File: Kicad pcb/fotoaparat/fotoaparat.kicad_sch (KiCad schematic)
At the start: 69 parts, among them IC1 Lineární Regulátor, IC2 Lineární Regulátor Displaye, J1 USB Konektor, J2 SWD, J3 LCD konektor, J4 Baterie, J5 Sd Karta, J6 UART, J7 Kamera, J8 Volné Piny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

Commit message: Buzzer
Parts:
- removed J8: Volné Piny, symbol Connector:Conn_01x12_Socket
- added BZ1: Buzzer, Inductor_SMD:L_SXN_SMDRI73, symbol Device:Buzzer
- added J9: Conn_01x11_Socket, symbol Connector:Conn_01x11_Socket
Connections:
- net -BATT: now also BZ1.2 (-)
- net pa10: now also J9.7 (Pin_7)
- net pa15: now also J9.3 (Pin_3)
- net pa2: now also J9.4 (Pin_4)
- net pa8: now also J9.5 (Pin_5)
- net pa9: now also J9.6 (Pin_6)
- net pb0: now also J9.2 (Pin_2)
- net pb1: now also J9.1 (Pin_1)
- net pb12: now also J9.10 (Pin_10)
- net pb14: now also J9.11 (Pin_11)
- net pc10: now also J9.8 (Pin_8)
- net pd2: now also J9.9 (Pin_9)
- net pb15 renamed buzzer
- net buzzer: now also BZ1.1 (+)
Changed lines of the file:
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@@
 	(wire
 		(pts
+			(xy 257.81 166.37) (xy 255.27 166.37)
+		)
+		(stroke
+			(width 0)
+			(type default)
+		)
+	)
+	(wire
+		(pts
 			(xy 129.54 55.88) (xy 116.84 55.88)
 		)
@@
 	(wire
 		(pts
-			(xy 179.07 161.29) (xy 252.73 161.29)
+			(xy 179.07 161.29) (xy 257.81 161.29)
 		)
 		(stroke
@@
 	(wire
 		(pts
-			(xy 252.73 161.29) (xy 252.73 135.89)
-		)
-		(stroke
-			(width 0)
-			(type default)
-		)
-	)
-	(wire
-		(pts
 			(xy -72.39 196.85) (xy -71.12 196.85)
 		)
@@
 	(wire
 		(pts
+			(xy 255.27 166.37) (xy 255.27 168.91)
+		)
+		(stroke
+			(width 0)
+			(type default)
+		)
+	)
+	(wire
+		(pts
 			(xy 154.94 31.75) (xy 163.83 31.75)
 		)
@@
 		)
 	)
-	(label "pb15"
-		(at 252.73 143.51 0)
+	(label "buzzer"
+		(at 251.46 161.29 0)
 		(effects
 			(font
@@
 	)
 	(symbol
+		(lib_id "Device:Buzzer")
+		(at 260.35 163.83 0)
+		(unit 1)
+		(exclude_from_sim no)
+		(in_bom yes)
+		(on_board yes)
+		(dnp no)
+		(fields_autoplaced yes)
+		(property "Reference" "BZ1"
+			(at 264.16 162.5599 0)
+			(effects
+				(font
+					(size 1.27 1.27)
+				)
+				(justify left)
+			)
+		)
+		(property "Value" "Buzzer"
+			(at 264.16 165.0999 0)
+			(effects
+				(font
+					(size 1.27 1.27)
+				)
+				(justify left)
+			)
+		)
+		(property "Footprint" "Inductor_SMD:L_SXN_SMDRI73"
+			(at 259.715 161.29 90)
+			(effects
+				(font
+					(size 1.27 1.27)
+				)
+				(hide yes)
+			)
+		)
+		(property "Datasheet" "~"
+			(at 259.715 161.29 90)
+			(effects
+				(font
+					(size 1.27 1.27)
+				)
+				(hide yes)
+			)
+		)
+		(property "Description" "Buzzer, polarized"
+			(at 260.35 163.83 0)
+			(effects
+				(font
+					(size 1.27 1.27)
+				)
+				(hide yes)
+			)
+		)
+		(pin "1"
+		)
+		(pin "2"
+		)
+		(instances
+			(project ""
+				(path "/af31909f-b2e8-4f24-bd61-08599f2fc290"
+					(reference "BZ1")
+					(unit 1)
+				)
+			)
+		)
+	)
+	(symbol
 		(lib_id "Device:R")
 		(at 68.58 72.39 0)
@@
 	)
 	(symbol
-		(lib_id "Connector:Conn_01x12_Socket")
-		(at 257.81 120.65 0)
-		(unit 1)
-		(exclude_from_sim no)
-		(in_bom yes)
-		(on_board yes)
-		(dnp no)
-		(fields_autoplaced yes)
-		(property "Reference" "J8"
-			(at 259.08 120.6499 0)
-			(effects
-				(font
-					(size 1.27 1.27)
-				)
-				(justify left)
-			)
-		)
-		(property "Value" "Volné Piny"
-			(at 259.08 123.1899 0)
-			(effects
-				(font
-					(size 1.27 1.27)
-				)
-				(justify left)
-			)
-		)
-		(property "Footprint" ""
-			(at 257.81 120.65 0)
-			(effects
-				(font
-					(size 1.27 1.27)
-				)
-				(hide yes)
-			)
-		)
-		(property "Datasheet" "~"
-			(at 257.81 120.65 0)
-			(effects
-				(font
-					(size 1.27 1.27)
-				)
-				(hide yes)
-			)
-		)
-		(property "Description" "Generic connector, single row, 01x12, script generated"
-			(at 257.81 120.65 0)
-			(effects
-				(font
-					(size 1.27 1.27)
-				)
-				(hide yes)
-			)
-		)
-		(pin "11"
-		)
-		(pin "1"
-		)
-		(pin "9"
-		)
-		(pin "2"
-		)
-		(pin "6"
-		)
-		(pin "10"
-		)
-		(pin "4"
-		)
-		(pin "3"
-		)
-		(pin "7"
-		)
-		(pin "5"
-		)
-		(pin "12"
-		)
-		(pin "8"
-		)
-		(instances
-			(project ""
-				(path "/af31909f-b2e8-4f24-bd61-08599f2fc290"
-					(reference "J8")
-					(unit 1)
-				)
-			)
-		)
-	)
-	(symbol
 		(lib_id "Device:C")
 		(at 97.79 76.2 90)
@@
 	)
 	(symbol
+		(lib_id "power:GND")
+		(at 255.27 168.91 0)
+		(unit 1)
+		(exclude_from_sim no)
+		(in_bom yes)
+		(on_board yes)
+		(dnp no)
+		(fields_autoplaced yes)
+		(property "Reference" "#PWR049"
+			(at 255.27 175.26 0)
+			(effects
+				(font
+					(size 1.27 1.27)
+				)
+				(hide yes)
+			)
+		)
+		(property "Value" "GND"
+			(at 255.27 173.99 0)
+			(effects
+				(font
+					(size 1.27 1.27)
+				)
+			)
+		)
+		(property "Footprint" ""
+			(at 255.27 168.91 0)
+			(effects
+				(font
+					(size 1.27 1.27)
+				)
+				(hide yes)
+			)
+		)
+		(property "Datasheet" ""
+			(at 255.27 168.91 0)
+			(effects
+				(font
+					(size 1.27 1.27)
+				)
+				(hide yes)
+			)
+		)
+		(property "Description" "Power symbol creates a global label with name \"GND\" , ground"
+			(at 255.27 168.91 0)
+			(effects
+				(font
+					(size 1.27 1.27)
+				)
+				(hide yes)
+			)
+		)
+		(pin "1"
+		)
+		(instances
+			(project ""
+				(path "/af31909f-b2e8-4f24-bd61-08599f2fc290"
+					(reference "#PWR049")
+					(unit 1)
+				)
+			)
+		)
+	)
+	(symbol
 		(lib_id "Device:R")
 		(at 207.01 31.75 0)
@@
 					(unit 1)
 				)
+			)
+		)
+	)
+	(symbol
+		(lib_id "Connector:Conn_01x11_Socket")
+		(at 257.81 120.65 0)
+		(unit 1)
+		(exclude_from_sim no)
+		(in_bom yes)
+		(on_board yes)
+		(dnp no)
+		(fields_autoplaced yes)
+		(property "Reference" "J9"
+			(at 259.08 119.3799 0)
+			(effects
+				(font
+					(size 1.27 1.27)
+				)
+				(justify left)
+			)
+		)
+		(property "Value" "Conn_01x11_Socket"
+			(at 259.08 121.9199 0)
+			(effects
+				(font
+					(size 1.27 1.27)
+				)
+				(justify left)
+			)
+		)
+		(property "Footprint" ""
+			(at 257.81 120.65 0)
+			(effects
+				(font
+					(size 1.27 1.27)
+				)
+				(hide yes)
+			)
+		)
+		(property "Datasheet" "~"
+			(at 257.81 120.65 0)
+			(effects
+				(font
+					(size 1.27 1.27)
+				)
+				(hide yes)
+			)
+		)
+		(property "Description" "Generic connector, single row, 01x11, script generated"
+			(at 257.81 120.65 0)
+			(effects
+				(font
+					(size 1.27 1.27)
+				)
+				(hide yes)
+			)
+		)
+		(pin "11"
+		)
+		(pin "6"
+		)
+		(pin "8"
+		)
+		(pin "2"
+		)
+		(pin "7"
+		)
+		(pin "10"
+		)
+		(pin "9"
+		)
+		(pin "4"
+		)
+		(pin "3"
+		)
+		(pin "1"
+		)
+		(pin "5"
+		)
+		(instances
+			(project ""
+				(path "/af31909f-b2e8-4f24-bd61-08599f2fc290"
+					(reference "J9")
+					(unit 1)
+				)

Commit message: Úprava knihoven
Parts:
- removed IC2: Lineární Regulátor Displaye, Package_TO_SOT_SMD:TSOT-23-5_HandSoldering, symbol NCP718ASN330T1G:NCP718ASN330T1G
- removed U3: Nabíječka baterie, MCP:MSOP10_MC_MCH, symbol 2025-09-30_17-20-56:MCP73833-FCI_UN
- added IC3: Lineární Regulátor Displaye, Package_TO_SOT_SMD:TSOT-23-5_HandSoldering, symbol NCP718ASN330T1G:NCP718ASN330T1G
- added U2: MCP73833-FCI/UN, MCP:MSOP10_MC_MCH, symbol 2025-09-30_17-20-56:MCP73833-FCI_UN
- J5: value Sd Karta -> GSD090012SEU
- S5: footprint cfs:CFS0201MB -> cfs201mb:CFS0201MB
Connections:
- net +3.3V LCD: now also IC3.5 (OUT)
- net +BATT: now also IC3.1 (IN), U2.10 (VBAT), U2.9 (VBAT)
- net VBUS: now also U2.1 (VDD), U2.2 (VDD)
- net scl: no longer J7.3 (Pin_3), R9.2, U1.29 (PB10)
- net sdo: no longer J7.4 (Pin_4), R10.2, U1.30 (PB11)
- net at R14.2, S1.6 (NO_2): now also IC3.3 (EN)
- net at R5.2: now also U2.4 (STAT2)
- net at R7.1: now also U2.6 (PROG)
- net im3: now reaches J3.14, R13.1
- net Vled+: now reaches J3.2, R8.2
- net at TH1.1: now also U2.8 (THERM)
- net at R6.2: now also U2.7 (*PG)
- net at R4.2: now also U2.3 (STAT1)
- net -BATT renamed GND
- net GND: now also IC3.2 (GND), U2.5 (VSS)
- new net I2C_SCL: J7.3 (Pin_3), R9.2, U1.29 (PB10)
- new net I2C_SDA: J7.4 (Pin_4), R10.2, U1.30 (PB11)
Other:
- moved on the sheet: R8

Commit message: Začátek návrhu pcb desky
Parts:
- added C21: 100n, Capacitor_SMD:C_0805_2012Metric_Pad1.18x1.45mm_HandSolder, symbol Device:C
- J9: footprint (none) -> Connector_PinSocket_2.54mm:PinSocket_1x11_P2.54mm_Horizontal
- R25, R26: footprint (none) -> Resistor_SMD:R_0805_2012Metric_Pad1.20x1.40mm_HandSolder
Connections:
- net +3.3V: now also C21.2; no longer R25.1
- net +BATT: now also R25.1
- net GND: now also C21.1
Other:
- moved on the sheet: C12

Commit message: Outline desky
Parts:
- added H1, H2, H3, H4: MountingHole, MountingHole:MountingHole_3.2mm_M3, symbol Mechanical:MountingHole

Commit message: První prototyp pcb
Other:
- moved on the sheet: H1, H2, H3, H4
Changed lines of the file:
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@@
 		(company "Vilem Maly")
 	)
+	(rectangle
+		(start -69.85 26.67)
+		(end -41.91 54.61)
+		(stroke
+			(width 0)
+			(type default)
+		)
+		(fill
+			(type none)
+		)
+	)
 	(text "Stm32 mikrokontrolér"
 		(exclude_from_sim no)
@@
 	(symbol
 		(lib_id "Mechanical:MountingHole")
-		(at -13.97 60.96 0)
+		(at -53.34 43.18 0)
 		(unit 1)
 		(exclude_from_sim no)
@@
 		(on_board yes)
 		(dnp no)
-		(fields_autoplaced yes)
 		(property "Reference" "H2"
-			(at -11.43 59.6899 0)
+			(at -54.356 46.228 0)
 			(effects
 				(font
@@
 		)
 		(property "Value" "MountingHole"
-			(at -11.43 62.2299 0)
+			(at -50.8 44.4499 0)
 			(effects
 				(font
@@
 				)
 				(justify left)
+				(hide yes)
 			)
 		)
 		(property "Footprint" "MountingHole:MountingHole_3.2mm_M3"
-			(at -13.97 60.96 0)
+			(at -53.34 43.18 0)
 			(effects
 				(font
@@
 		)
 		(property "Datasheet" "~"
-			(at -13.97 60.96 0)
+			(at -53.34 43.18 0)
 			(effects
 				(font
@@
 		)
 		(property "Description" "Mounting Hole without connection"
-			(at -13.97 60.96 0)
+			(at -53.34 43.18 0)
 			(effects
 				(font
@@
 	(symbol
 		(lib_id "Mechanical:MountingHole")
-		(at -20.32 60.96 0)
+		(at -59.69 43.18 0)
 		(unit 1)
 		(exclude_from_sim no)
@@
 		(on_board yes)
 		(dnp no)
-		(fields_autoplaced yes)
 		(property "Reference" "H4"
-			(at -17.78 59.6899 0)
+			(at -60.96 46.228 0)
 			(effects
 				(font
@@
 		)
 		(property "Value" "MountingHole"
-			(at -17.78 62.2299 0)
+			(at -57.15 44.4499 0)
 			(effects
 				(font
@@
 				)
 				(justify left)
+				(hide yes)
 			)
 		)
 		(property "Footprint" "MountingHole:MountingHole_3.2mm_M3"
-			(at -20.32 60.96 0)
+			(at -59.69 43.18 0)
 			(effects
 				(font
@@
 		)
 		(property "Datasheet" "~"
-			(at -20.32 60.96 0)
+			(at -59.69 43.18 0)
 			(effects
 				(font
@@
 		)
 		(property "Description" "Mounting Hole without connection"
-			(at -20.32 60.96 0)
+			(at -59.69 43.18 0)
 			(effects
 				(font
@@
 	(symbol
 		(lib_id "Mechanical:MountingHole")
-		(at -13.97 55.88 0)
+		(at -53.34 38.1 0)
 		(unit 1)
 		(exclude_from_sim no)
@@
 		(on_board yes)
 		(dnp no)
-		(fields_autoplaced yes)
 		(property "Reference" "H1"
-			(at -11.43 54.6099 0)
+			(at -54.61 35.052 0)
 			(effects
 				(font
@@
 		)
 		(property "Value" "MountingHole"
-			(at -11.43 57.1499 0)
+			(at -50.8 39.3699 0)
 			(effects
 				(font
@@
 				)
 				(justify left)
+				(hide yes)
 			)
 		)
 		(property "Footprint" "MountingHole:MountingHole_3.2mm_M3"
-			(at -13.97 55.88 0)
+			(at -53.34 38.1 0)
 			(effects
 				(font
@@
 		)
 		(property "Datasheet" "~"
-			(at -13.97 55.88 0)
+			(at -53.34 38.1 0)
 			(effects
 				(font
@@
 		)
 		(property "Description" "Mounting Hole without connection"
-			(at -13.97 55.88 0)
+			(at -53.34 38.1 0)
 			(effects
 				(font
@@
 	(symbol
 		(lib_id "Mechanical:MountingHole")
-		(at -20.32 55.88 0)
+		(at -59.69 38.1 0)
 		(unit 1)
 		(exclude_from_sim no)
@@
 		(on_board yes)
 		(dnp no)
-		(fields_autoplaced yes)
 		(property "Reference" "H3"
-			(at -17.78 54.6099 0)
+			(at -61.468 35.306 0)
 			(effects
 				(font
@@
 		)
 		(property "Value" "MountingHole"
-			(at -17.78 57.1499 0)
+			(at -74.168 38.354 0)
 			(effects
 				(font
@@
 				)
 				(justify left)
+				(hide yes)
 			)
 		)
 		(property "Footprint" "MountingHole:MountingHole_3.2mm_M3"
-			(at -20.32 55.88 0)
+			(at -59.69 38.1 0)
 			(effects
 				(font
@@
 		)
 		(property "Datasheet" "~"
-			(at -20.32 55.88 0)
+			(at -59.69 38.1 0)
 			(effects
 				(font
@@
 		)
 		(property "Description" "Mounting Hole without connection"
-			(at -20.32 55.88 0)
+			(at -59.69 38.1 0)
 			(effects
 				(font

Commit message: Drobné změny
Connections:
- net Backlight Regulátor renamed Backlight Regulátor en
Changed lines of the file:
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@@
 	(wire
 		(pts
+			(xy -43.18 128.27) (xy -36.83 128.27)
+		)
+		(stroke
+			(width 0)
+			(type default)
+		)
+	)
+	(wire
+		(pts
 			(xy 250.19 113.03) (xy 252.73 113.03)
 		)
@@
 	)
 	(label "pb1"
-		(at 252.73 105.41 0)
+		(at 252.73 107.95 0)
 		(effects
 			(font
@@
 	)
 	(label "sd mosi"
-		(at 171.45 68.58 0)
+		(at 224.79 59.69 0)
 		(effects
 			(font
@@
 	)
 	(label "pb12"
-		(at 250.19 148.59 0)
+		(at 250.19 130.81 0)
 		(effects
 			(font
@@
 	)
 	(label "sd cs"
-		(at 201.93 58.42 0)
+		(at 224.79 57.15 0)
 		(effects
 			(font
@@
 	)
 	(label "csx"
-		(at 181.61 101.6 0)
+		(at 187.96 129.54 0)
 		(effects
 			(font
@@
 	)
 	(label "pb14"
-		(at 251.46 139.7 0)
+		(at 251.46 133.35 0)
 		(effects
 			(font
@@
 	)
 	(label "USB_D-"
-		(at 170.18 78.74 0)
+		(at 180.34 78.74 0)
 		(effects
 			(font
@@
 	)
 	(label "swdio"
-		(at 170.18 83.82 0)
+		(at 231.14 91.44 0)
 		(effects
 			(font
@@
 	)
 	(label "swclk"
-		(at 170.18 86.36 0)
+		(at 231.14 93.98 0)
 		(effects
 			(font
@@
 	)
 	(label "boot0"
-		(at 86.36 60.96 0)
+		(at 80.01 60.96 0)
 		(effects
 			(font
@@
 	)
 	(label "sd clk"
-		(at 200.66 63.5 0)
+		(at 224.79 67.31 0)
 		(effects
 			(font
@@
 	)
 	(label "sd miso"
-		(at 189.23 104.14 0)
+		(at 220.98 72.39 0)
 		(effects
 			(font
@@
 	)
 	(label "rrst"
-		(at 107.95 116.84 0)
+		(at 106.68 116.84 0)
 		(effects
 			(font
@@
 	)
 	(label "scl"
-		(at 208.28 110.49 0)
+		(at 218.44 127 0)
 		(effects
 			(font
@@
 	)
 	(label "href"
-		(at 109.22 96.52 0)
+		(at 107.95 96.52 0)
 		(effects
 			(font
@@
 	)
 	(label "pa15"
-		(at 237.49 100.33 0)
+		(at 250.19 113.03 0)
 		(effects
 			(font
@@
 	)
 	(label "I2C_SCL"
-		(at 86.36 93.98 0)
+		(at 82.55 93.98 0)
 		(effects
 			(font
@@
 	)
 	(label "rst"
-		(at 198.12 99.06 0)
+		(at 218.44 124.46 0)
 		(effects
 			(font
@@
 	)
 	(label "wr"
-		(at 90.17 120.65 0)
+		(at 90.17 114.3 0)
 		(effects
 			(font
@@
 	)
 	(label "uart tx"
-		(at 179.07 50.8 0)
+		(at 180.34 50.8 0)
 		(effects
 			(font
@@
 	)
 	(label "wrst"
-		(at 102.87 119.38 0)
+		(at 92.71 119.38 0)
 		(effects
 			(font
@@
 	)
 	(label "sda"
-		(at 184.15 127 0)
+		(at 187.96 127 0)
 		(effects
 			(font
@@
 		)
 	)
-	(label "Backlight Regulátor"
+	(label "Backlight Regulátor en"
 		(at -60.96 158.75 0)
 		(effects
@@
 	)
 	(label "I2C_SDA"
-		(at 109.22 93.98 0)
+		(at 107.95 93.98 0)
 		(effects
 			(font
@@
 	)
 	(label "Reset"
-		(at 123.19 50.8 0)
+		(at 111.76 53.34 0)
 		(effects
 			(font
@@
 	)
 	(label "pb0"
-		(at 240.03 104.14 0)
+		(at 251.46 110.49 0)
 		(effects
 			(font
@@
 	)
 	(label "wrx d{slash}cx"
-		(at 190.5 107.95 0)
+		(at 219.71 129.54 0)
 		(effects
 			(font
@@
 	)
 	(label "USB_D+"
-		(at 170.18 81.28 0)
+		(at 180.34 81.28 0)
 		(effects
 			(font
@@
 	)
 	(label "sdo"
-		(at 189.23 152.4 0)
+		(at 219.71 132.08 0)
 		(effects
 			(font
@@
 		(on_board yes)
 		(dnp no)
-		(fields_autoplaced yes)
 		(property "Reference" "#PWR023"
 			(at 114.3 91.44 0)
@@
 		)
 		(property "Value" "GND"
-			(at 111.76 91.4399 90)
+			(at 110.49 89.662 90)
 			(effects
 				(font
@@
 		)
 		(property "Value" "+3.3V"
-			(at 230.886 89.916 0)
+			(at 230.632 85.09 0)
 			(effects
 				(font
@@
 					(unit 1)
 				)
+			)
+		)
+	)
+	(symbol
+		(lib_id "power:PWR_FLAG")
+		(at -36.83 128.27 0)
+		(unit 1)
+		(exclude_from_sim no)
+		(in_bom yes)
+		(on_board yes)
+		(dnp no)
+		(fields_autoplaced yes)
+		(property "Reference" "#FLG02"
+			(at -36.83 126.365 0)
+			(effects
+				(font
+					(size 1.27 1.27)
+				)
+				(hide yes)
+			)
+		)
+		(property "Value" "PWR_FLAG"
+			(at -36.83 123.19 0)
+			(effects
+				(font
+					(size 1.27 1.27)
+				)
+			)
+		)
+		(property "Footprint" ""
+			(at -36.83 128.27 0)
+			(effects
+				(font
+					(size 1.27 1.27)
+				)
+				(hide yes)
+			)
+		)
+		(property "Datasheet" "~"
+			(at -36.83 128.27 0)
+			(effects
+				(font
+					(size 1.27 1.27)
+				)
+				(hide yes)
+			)
+		)
+		(property "Description" "Special symbol for telling ERC where power comes from"
+			(at -36.83 128.27 0)
+			(effects
+				(font
+					(size 1.27 1.27)
+				)
+				(hide yes)
+			)
+		)
+		(pin "1"
+		)
+		(instances
+			(project ""
+				(path "/af31909f-b2e8-4f24-bd61-08599f2fc290"
+					(reference "#FLG02")
+					(unit 1)
+				)

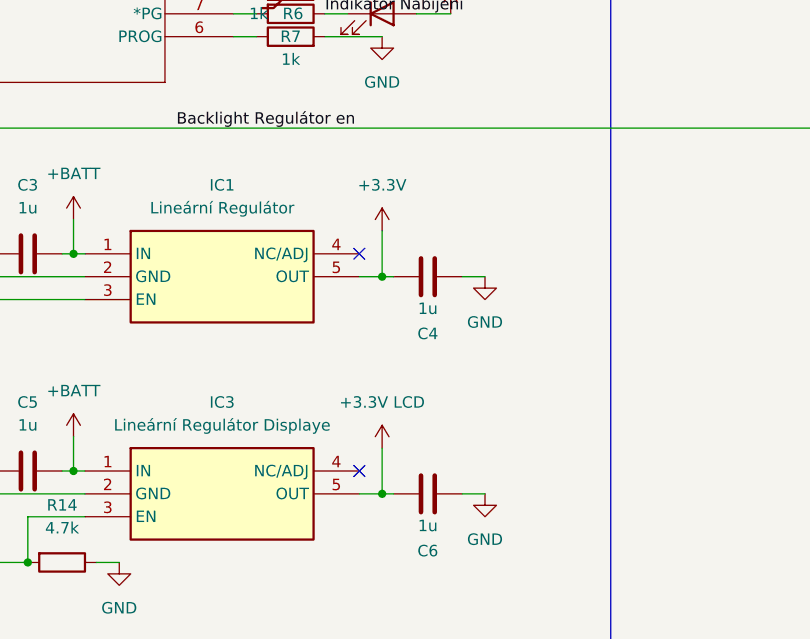
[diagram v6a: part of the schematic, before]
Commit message: Druhá deska pcb
Signálové trasy jsou víc daleko od sebe a napájecí trasy jsou více široké než v minulém designu, to by mělo zmírnit elektromagnetickou interferenci.
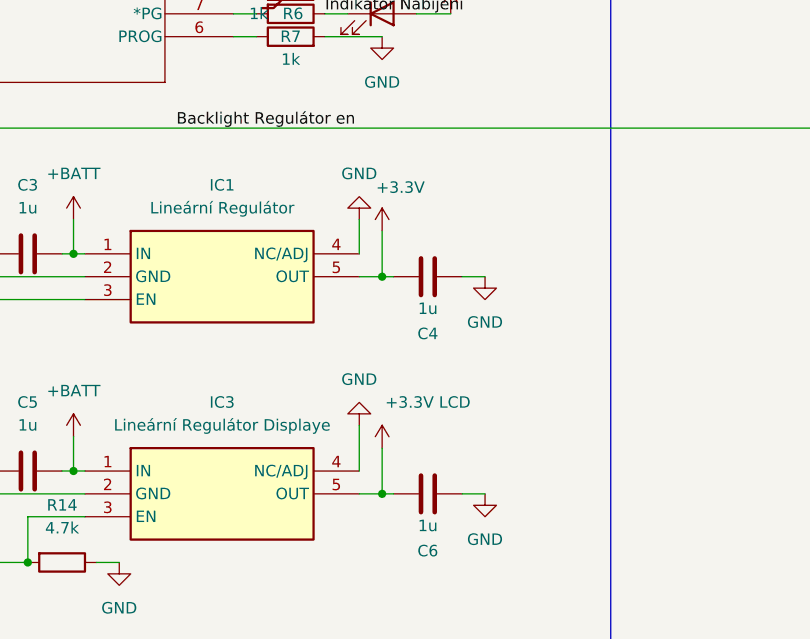
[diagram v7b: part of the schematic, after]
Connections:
- net GND: now also IC1.4 (NC/ADJ), IC3.4 (NC/ADJ)
- no-connect marks 37 -> 35
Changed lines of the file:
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@@
 	)
 	(no_connect
-		(at -40.64 196.85)
-	)
-	(no_connect
 		(at 271.78 72.39)
 	)
@@
 	)
 	(no_connect
-		(at -40.64 172.72)
-	)
-	(no_connect
 		(at -113.03 204.47)
 	)
@@
 	(wire
 		(pts
+			(xy -40.64 191.77) (xy -40.64 196.85)
+		)
+		(stroke
+			(width 0)
+			(type default)
+		)
+	)
+	(wire
+		(pts
 			(xy 80.01 60.96) (xy 129.54 60.96)
 		)
@@
 	(wire
 		(pts
+			(xy -40.64 168.91) (xy -40.64 172.72)
+		)
+		(stroke
+			(width 0)
+			(type default)
+		)
+	)
+	(wire
+		(pts
 			(xy 105.41 91.44) (xy 106.68 91.44)
 		)
@@
 		(on_board yes)
 		(dnp no)
-		(fields_autoplaced yes)
 		(property "Reference" "#PWR0101"
 			(at -38.1 198.12 0)
@@
 		)
 		(property "Value" "+3.3V LCD"
-			(at -38.1 189.23 0)
+			(at -33.02 189.23 0)
 			(effects
 				(font
@@
 	)
 	(symbol
+		(lib_id "power:GND")
+		(at -40.64 168.91 180)
+		(unit 1)
+		(exclude_from_sim no)
+		(in_bom yes)
+		(on_board yes)
+		(dnp no)
+		(fields_autoplaced yes)
+		(property "Reference" "#PWR021"
+			(at -40.64 162.56 0)
+			(effects
+				(font
+					(size 1.27 1.27)
+				)
+				(hide yes)
+			)
+		)
+		(property "Value" "GND"
+			(at -40.64 163.83 0)
+			(effects
+				(font
+					(size 1.27 1.27)
+				)
+			)
+		)
+		(property "Footprint" ""
+			(at -40.64 168.91 0)
+			(effects
+				(font
+					(size 1.27 1.27)
+				)
+				(hide yes)
+			)
+		)
+		(property "Datasheet" ""
+			(at -40.64 168.91 0)
+			(effects
+				(font
+					(size 1.27 1.27)
+				)
+				(hide yes)
+			)
+		)
+		(property "Description" "Power symbol creates a global label with name \"GND\" , ground"
+			(at -40.64 168.91 0)
+			(effects
+				(font
+					(size 1.27 1.27)
+				)
+				(hide yes)
+			)
+		)
+		(pin "1"
+		)
+		(instances
+			(project ""
+				(path "/af31909f-b2e8-4f24-bd61-08599f2fc290"
+					(reference "#PWR021")
+					(unit 1)
+				)
+			)
+		)
+	)
+	(symbol
 		(lib_id "Device:C")
 		(at 176.53 38.1 0)
@@
 	)
 	(symbol
+		(lib_id "power:GND")
+		(at -40.64 191.77 180)
+		(unit 1)
+		(exclude_from_sim no)
+		(in_bom yes)
+		(on_board yes)
+		(dnp no)
+		(fields_autoplaced yes)
+		(property "Reference" "#PWR035"
+			(at -40.64 185.42 0)
+			(effects
+				(font
+					(size 1.27 1.27)
+				)
+				(hide yes)
+			)
+		)
+		(property "Value" "GND"
+			(at -40.64 186.69 0)
+			(effects
+				(font
+					(size 1.27 1.27)
+				)
+			)
+		)
+		(property "Footprint" ""
+			(at -40.64 191.77 0)
+			(effects
+				(font
+					(size 1.27 1.27)
+				)
+				(hide yes)
+			)
+		)
+		(property "Datasheet" ""
+			(at -40.64 191.77 0)
+			(effects
+				(font
+					(size 1.27 1.27)
+				)
+				(hide yes)
+			)
+		)
+		(property "Description" "Power symbol creates a global label with name \"GND\" , ground"
+			(at -40.64 191.77 0)
+			(effects
+				(font
+					(size 1.27 1.27)
+				)
+				(hide yes)
+			)
+		)
+		(pin "1"
+		)
+		(instances
+			(project ""
+				(path "/af31909f-b2e8-4f24-bd61-08599f2fc290"
+					(reference "#PWR035")
+					(unit 1)
+				)
+			)
+		)
+	)
+	(symbol
 		(lib_id "power:PWR_FLAG")
 		(at 163.83 29.21 0)
@@
 		(on_board yes)
 		(dnp no)
-		(fields_autoplaced yes)
 		(property "Reference" "#PWR040"
 			(at -38.1 173.99 0)
@@
 		)
 		(property "Value" "+3.3V"
-			(at -38.1 165.1 0)
+			(at -36.068 165.354 0)
 			(effects
 				(font

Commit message: Příprava na výrobu pcb
Gerber soubory se pravděpodobně ještě změní
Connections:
- net d0: now also U1.38 (PC7); no longer U1.37 (PC6)
- net d1: now also U1.37 (PC6); no longer U1.38 (PC7)
- net d2: now also U1.40 (PC9); no longer U1.39 (PC8)
- net d3: now also U1.39 (PC8); no longer U1.40 (PC9)
- net d4: now also U1.58 (PB6); no longer U1.52 (PC11)
- net d5: now also U1.52 (PC11); no longer U1.58 (PB6)
- net d6: now also U1.62 (PB9); no longer U1.61 (PB8)
- net d7: now also U1.61 (PB8); no longer U1.62 (PB9)
- net href: now also U1.59 (PB7); no longer U1.20 (PA4)
- net rrst: now also U1.3 (PC14); no longer U1.2 (PC13)
- net vsync: now also U1.20 (PA4); no longer U1.59 (PB7)
- net wrst: now also U1.2 (PC13); no longer U1.3 (PC14)
